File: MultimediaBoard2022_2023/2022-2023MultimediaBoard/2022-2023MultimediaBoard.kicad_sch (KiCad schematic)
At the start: 16 parts, among them J1 Conn_02x02_Counter_Clockwise_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, J2 RJ45_LED_Shielded_Ethernet, J3 Conn_02x03_Counter_Clockwise, U2 OKI, U3 Teensy4.1_DEV-16771

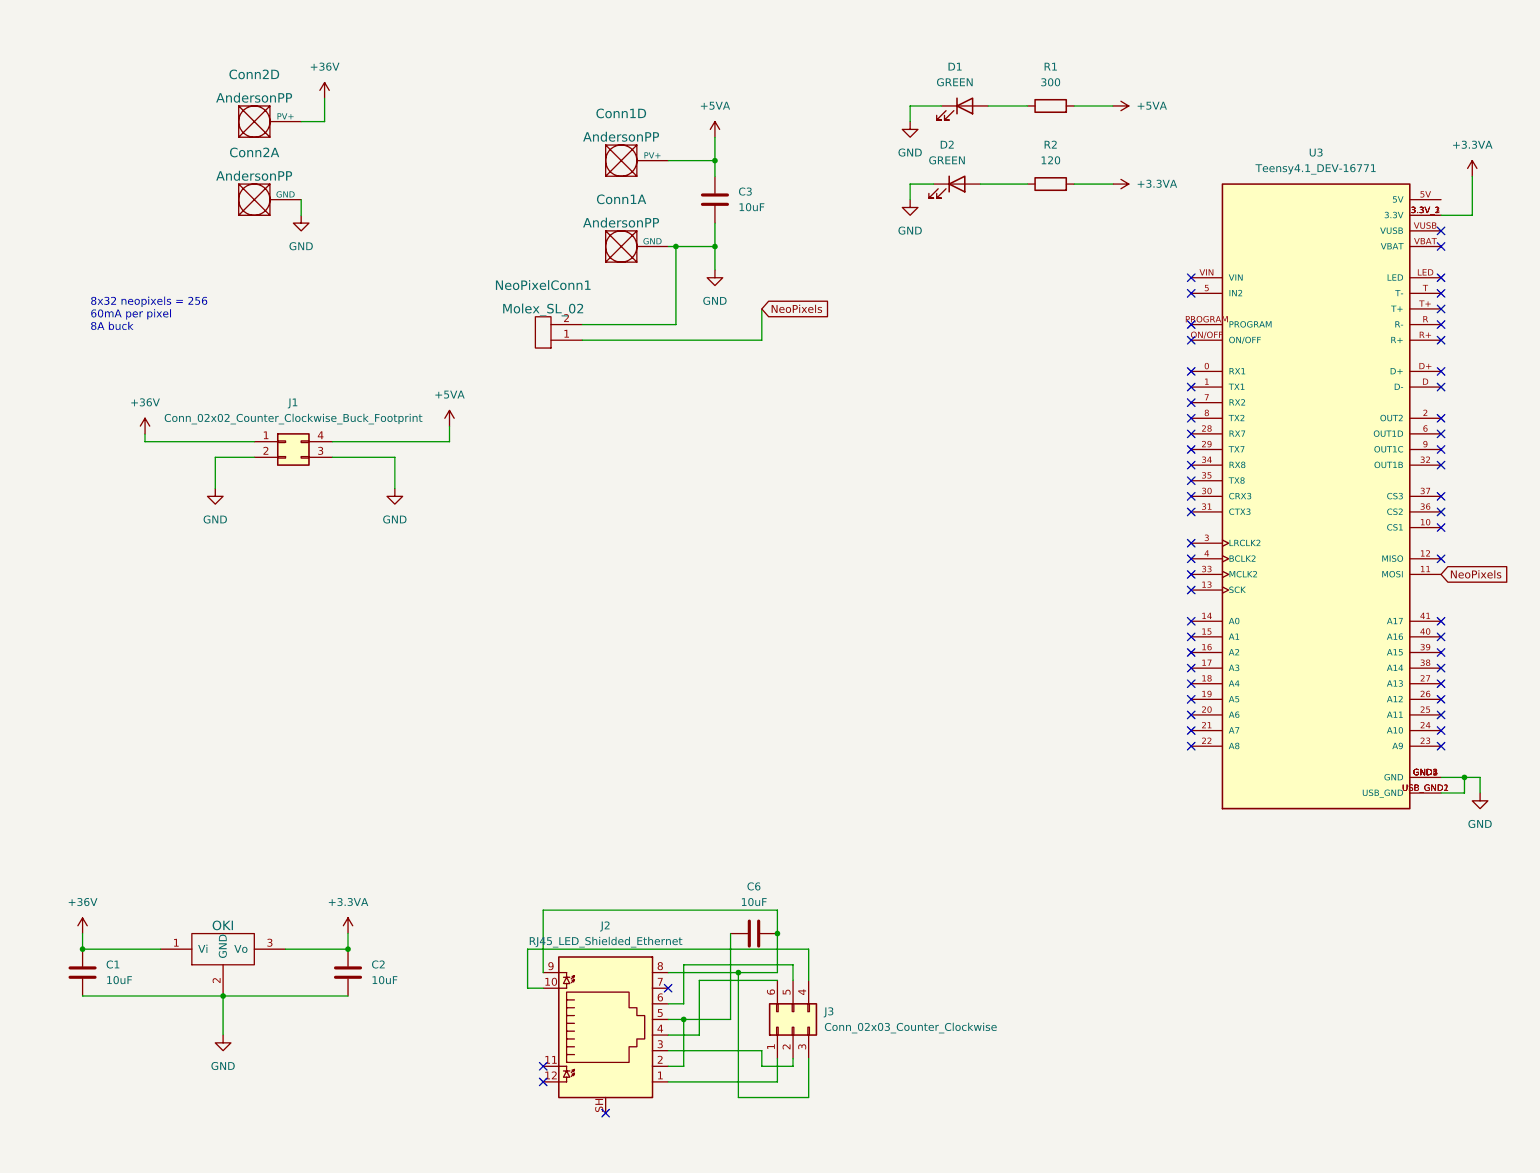
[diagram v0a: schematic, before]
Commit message: Sectioned parts of schematic, changed power sources, grounded LEDs
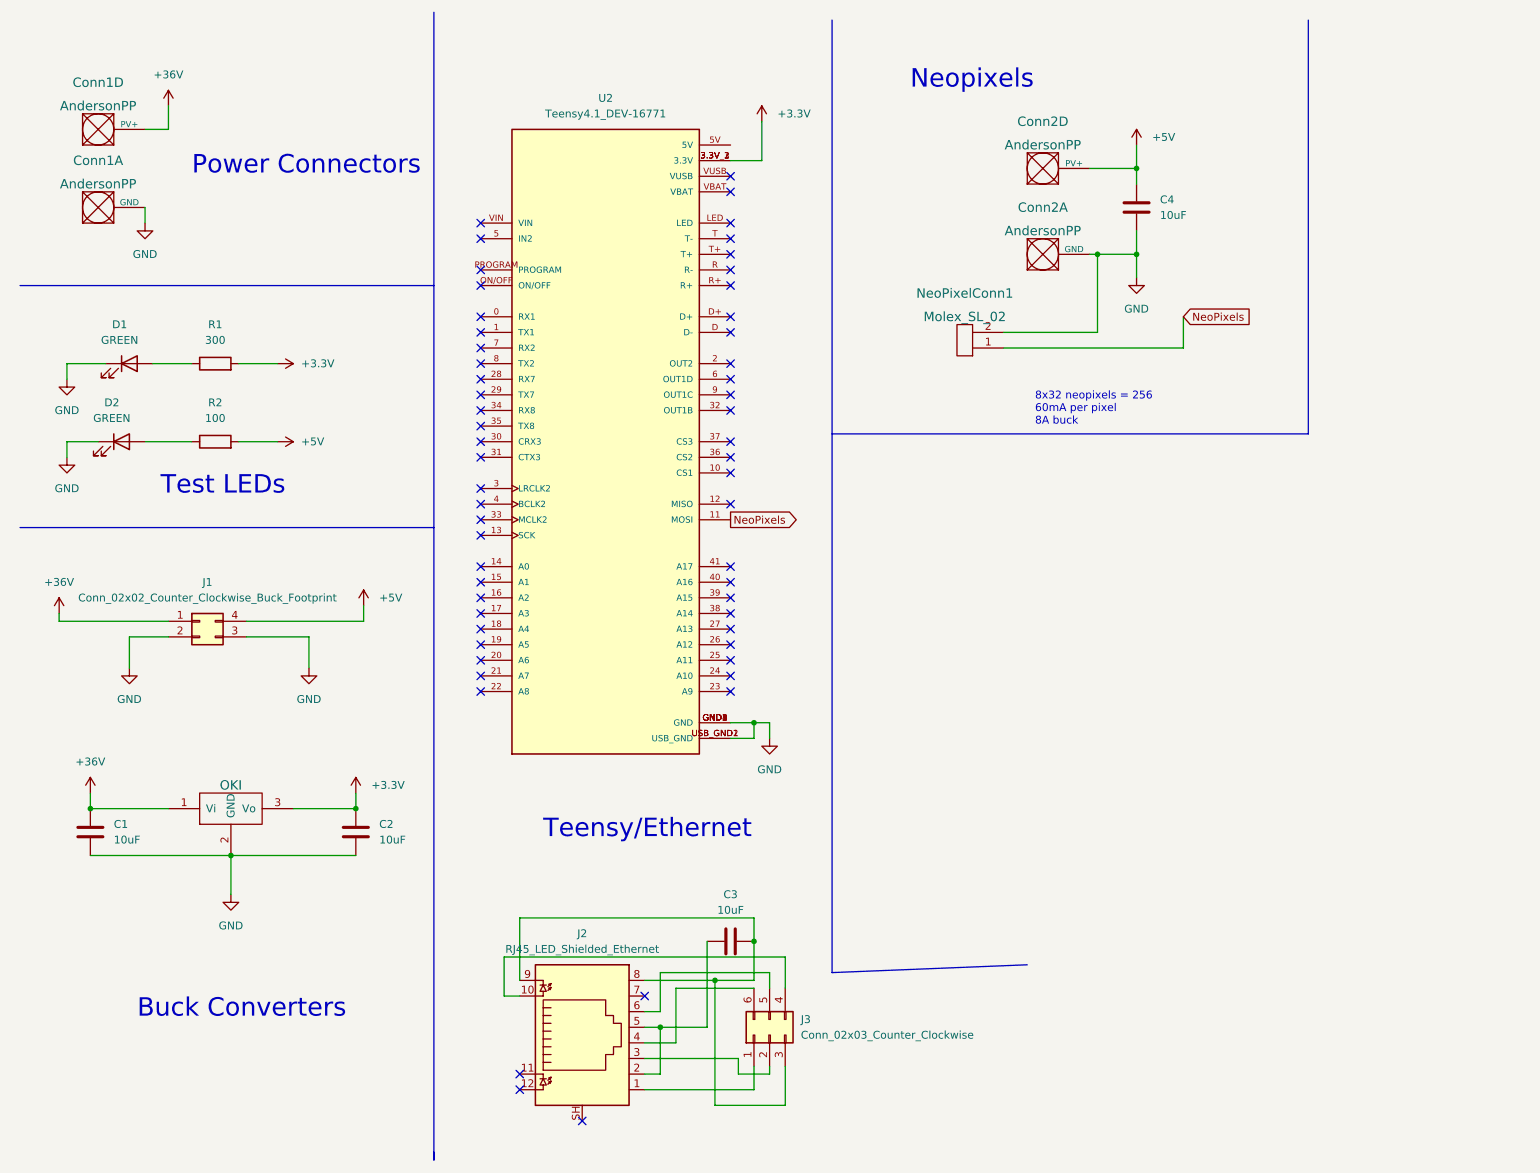
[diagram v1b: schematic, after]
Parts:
- removed C6: 10uF, Capacitor_SMD:C_0603_1608Metric_Pad1.08x0.95mm_HandSolder, symbol Device:C
- removed U2: OKI, MRDT_Devices:OKI_Horizontal, symbol MRDT_Devices:OKI
- removed U3: Teensy4.1_DEV-16771, MRDT_Shields:MODULE_DEV-16771, symbol MRDT_Shields:Teensy4.1_DEV-16771
- added C4: 10uF, symbol Device:C
- added U1: OKI, symbol MRDT_Devices:OKI
- added U2: Teensy4.1_DEV-16771, MODULE_DEV-16771, symbol MRDT_Shields:Teensy4.1_DEV-16771
- C1, C2, C3: footprint Capacitor_SMD:C_0603_1608Metric_Pad1.08x0.95mm_HandSolder -> (none)
- Conn1, Conn2: footprint MRDT_Connectors:Square_Anderson_2_H_Side_By_Side_PV -> (none)
- D1, D2: footprint LED_SMD:LED_0603_1608Metric_Pad1.05x0.95mm_HandSolder -> (none)
- J1: footprint Connector_PinHeader_2.00mm:PinHeader_2x02_P2.00mm_Vertical -> (none)
- J2: footprint MRDT_Connectors:RJ45_Teensy -> (none)
- J3: footprint Connector_PinHeader_2.00mm:PinHeader_2x03_P2.00mm_Vertical -> (none)
- NeoPixelConn1: footprint MRDT_Connectors:MOLEX_SL_02_Horizontal -> (none)
- R1: footprint Resistor_SMD:R_0201_0603Metric_Pad0.64x0.40mm_HandSolder -> (none)
- R2: value 120 -> 100; footprint Resistor_SMD:R_0201_0603Metric_Pad0.64x0.40mm_HandSolder -> (none)
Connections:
- net +36V: now also Conn1.4 (PV+), U1.1 (Vi); no longer Conn2.4 (PV+)
- net GND: now also C4.2, U1.2 (GND), U2.GND1 (GND), U2.GND2 (GND), U2.GND3 (GND), U2.GND4 (GND), U2.GND5 (GND), U2.USB_GND1 (USB_GND), U2.USB_GND2 (USB_GND); no longer C3.2
- net NeoPixels: now also U2.11 (MOSI)
- net at J2.8, J2.9, J3.3 (Pin_3): now also C3.1
- net at J2.2, J2.5: now also C3.2
- net +3.3VA renamed +3.3V
- net +3.3V: now also R1.2, U1.3 (Vo), U2.3.3V_1 (3.3V), U2.3.3V_2 (3.3V), U2.3.3V_3 (3.3V); no longer R2.2
- removed net +5VA: C3.1, Conn1.4 (PV+), J1.4 (Pin_4), R1.2
- new net +5V: C4.1, Conn2.4 (PV+), J1.4 (Pin_4), R2.2
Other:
- note added: "Buck Converters"
- note added: "Neopixels"
- note added: "Power Connectors"
- note added: "Teensy/Ethernet"
- note added: "Test LEDs"

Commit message: Renamed buck converter, minor touchups
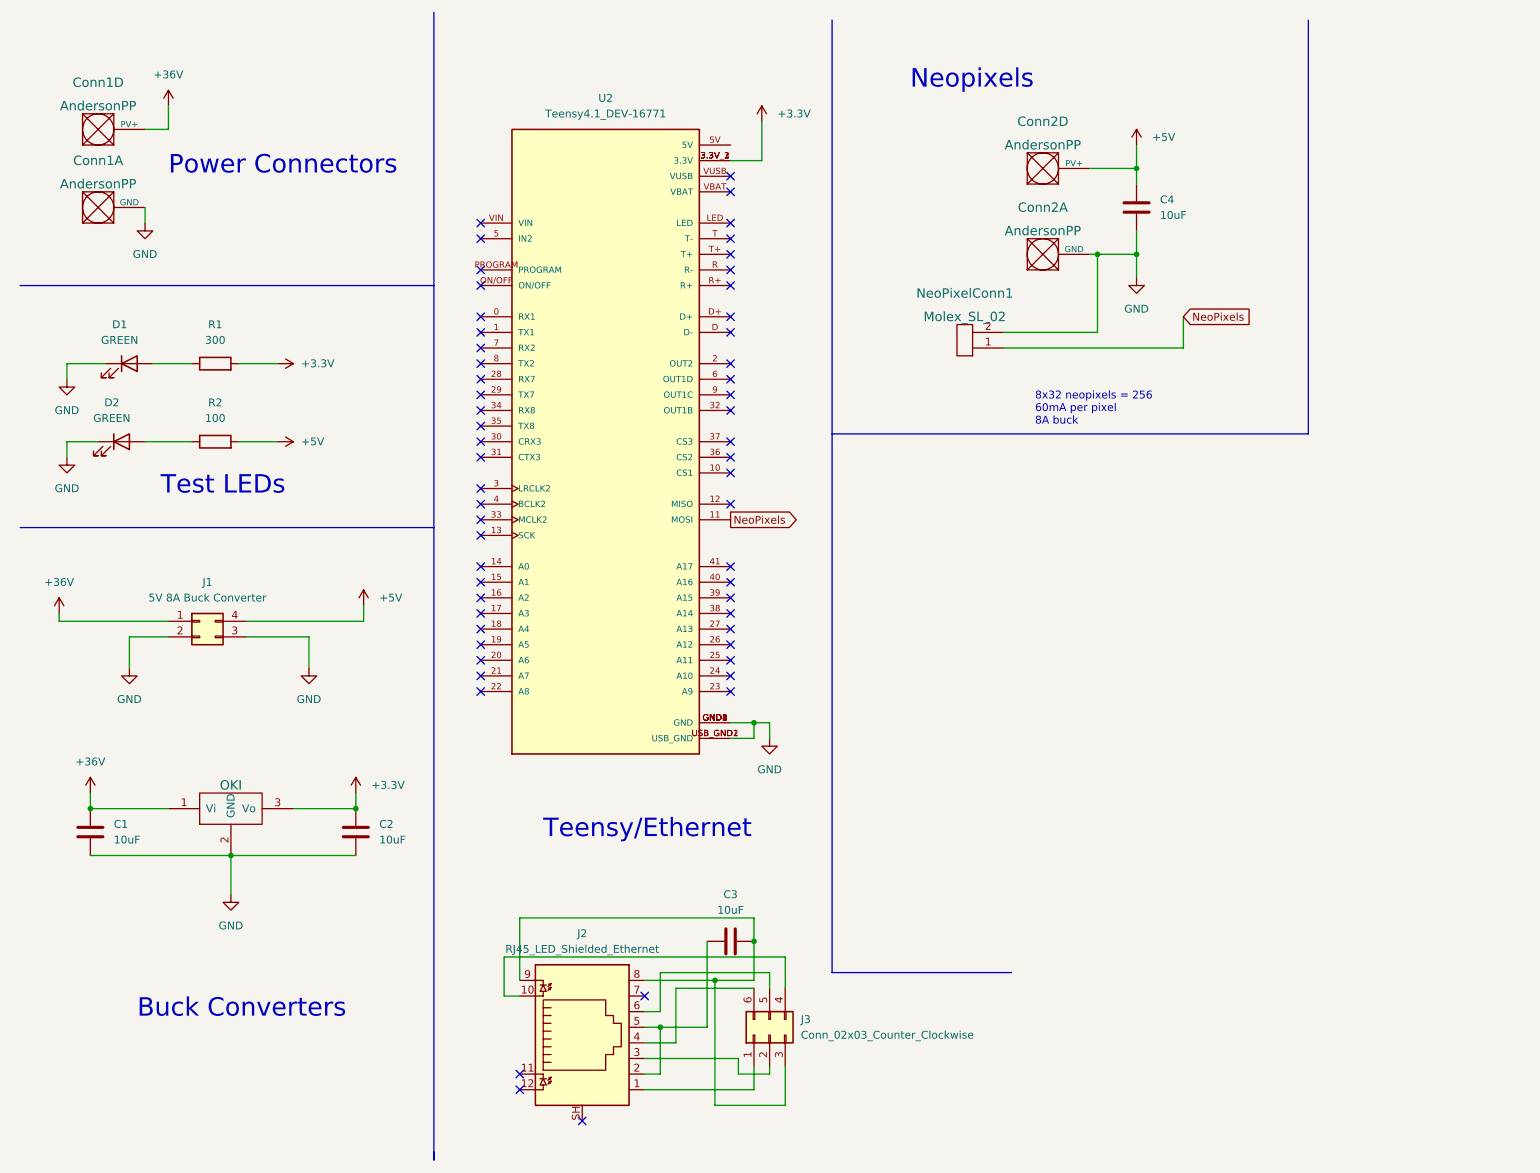
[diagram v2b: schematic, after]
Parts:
- J1: value Conn_02x02_Counter_Clockwise_Buck_Footprint -> 5V 8A Buck Converter
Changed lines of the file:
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@@
+    (stroke (width 0) (type default) (color 0 0 0 0))
+  )
+  (polyline (pts (xy 148.59 167.64) (xy 176.53 167.64))
     (stroke (width 0) (type default) (color 0 0 0 0))
   )
@@
     (stroke (width 0) (type default) (color 0 0 0 0))
   )
-  (polyline (pts (xy 147.32 167.64) (xy 179.07 166.37))
-    (stroke (width 0) (type default) (color 0 0 0 0))
-  )
   (wire (pts (xy 93.98 171.45) (xy 96.52 171.45))
     (stroke (width 0) (type default) (color 0 0 0 0))
@@
   )
   (wire (pts (xy 33.02 113.03) (xy 33.02 118.11))
+    (stroke (width 0) (type default) (color 0 0 0 0))
+  )
+  (polyline (pts (xy 147.32 167.64) (xy 148.59 167.64))
     (stroke (width 0) (type default) (color 0 0 0 0))
   )
@@
     (effects (font (size 3 3)) (justify left bottom))
   )
-  (text "Power Connectors" (at 43.18 38.1 0)
+  (text "Power Connectors" (at 39.37 38.1 0)
     (effects (font (size 3 3)) (justify left bottom))
   )
@@
     (in_bom yes) (on_board yes) (fields_autoplaced)
     (property "Reference" "J1" (id 0) (at 45.72 104.14 0))
-    (property "Value" "Conn_02x02_Counter_Clockwise_Buck_Footprint" (id 1) (at 45.72 106.68 0))
+    (property "Value" "5V 8A Buck Converter" (id 1) (at 45.72 106.68 0))
     (property "Footprint" "" (id 2) (at 44.45 110.49 0)
       (effects (font (size 1.27 1.27)) hide)
@@
     )
     (path "/9e2b21a3-05cc-4e86-bc90-cb131a45fd36"
-      (reference "J1") (unit 1) (value "Conn_02x02_Counter_Clockwise_Buck_Footprint") (footprint "")
+      (reference "J1") (unit 1) (value "5V 8A Buck Converter") (footprint "")
     )
     (path "/01d7ed54-9442-442b-bc84-39ad0e7c7375"

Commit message: Quick fixes, new BOM
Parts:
- C1: renamed from C4; footprint (none) -> Capacitor_SMD:C_0603_1608Metric_Pad1.08x0.95mm_HandSolder
- C2: renamed from C1; footprint (none) -> Capacitor_SMD:C_0603_1608Metric_Pad1.08x0.95mm_HandSolder
- C3: renamed from C2; footprint (none) -> Capacitor_SMD:C_0603_1608Metric_Pad1.08x0.95mm_HandSolder
- C4: renamed from C3; footprint (none) -> Capacitor_SMD:C_0603_1608Metric_Pad1.08x0.95mm_HandSolder
- Conn1, Conn2: footprint (none) -> MRDT_Connectors:Square_Anderson_2_H_Side_By_Side_PV
- D1, D2: footprint (none) -> LED_SMD:LED_0603_1608Metric_Pad1.05x0.95mm_HandSolder
- J1: footprint (none) -> Connector_PinHeader_2.00mm:PinHeader_2x02_P2.00mm_Vertical
- J2: renamed from J3; footprint (none) -> Connector_PinHeader_2.00mm:PinHeader_2x03_P2.00mm_Vertical
- J3: renamed from J2; footprint (none) -> MRDT_Connectors:RJ45_Teensy
- NeoPixelConn1: footprint (none) -> MRDT_Connectors:MOLEX_SL_02_Horizontal
- R1, R2: footprint (none) -> Resistor_SMD:R_0201_0603Metric_Pad0.64x0.40mm_HandSolder
- U1: renamed from U2; footprint MODULE_DEV-16771 -> MRDT_Shields:Teensy_4_1_Vertical
- U2: renamed from U1; footprint (none) -> MRDT_Devices:OKI_Horizontal
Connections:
- net Tx+: now reaches J2.1 (Pin_1), J3.1
- net Tx-: now reaches J2.2 (Pin_2), J3.3
- net Rx+: now reaches J2.6 (Pin_6), J3.4
- net Rx-: now reaches J2.5 (Pin_5), J3.6
- no-connect marks 57 -> 58
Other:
- moved on the sheet: Conn1D, U1

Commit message: PCB edits and footprint assignment
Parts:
- J1: footprint Connector_PinHeader_2.00mm:PinHeader_2x02_P2.00mm_Vertical -> MultimediaBoard2023:5V 8A Buck Converter
- R1, R2: footprint Resistor_SMD:R_0201_0603Metric_Pad0.64x0.40mm_HandSolder -> Resistor_SMD:R_0603_1608Metric_Pad0.98x0.95mm_HandSolder
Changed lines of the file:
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@@
     (property "Reference" "R2" (id 0) (at 46.99 74.93 90))
     (property "Value" "100" (id 1) (at 46.99 77.47 90))
-    (property "Footprint" "Resistor_SMD:R_0201_0603Metric_Pad0.64x0.40mm_HandSolder" (id 2) (at 46.99 83.058 90)
+    (property "Footprint" "Resistor_SMD:R_0603_1608Metric_Pad0.98x0.95mm_HandSolder" (id 2) (at 46.99 83.058 90)
       (effects (font (size 1.27 1.27)) hide)
     )
@@
     (property "Reference" "R1" (id 0) (at 46.99 62.23 90))
     (property "Value" "300" (id 1) (at 46.99 64.77 90))
-    (property "Footprint" "Resistor_SMD:R_0201_0603Metric_Pad0.64x0.40mm_HandSolder" (id 2) (at 46.99 70.358 90)
+    (property "Footprint" "Resistor_SMD:R_0603_1608Metric_Pad0.98x0.95mm_HandSolder" (id 2) (at 46.99 70.358 90)
       (effects (font (size 1.27 1.27)) hide)
     )
@@
     (property "Reference" "J1" (id 0) (at 45.72 104.14 0))
     (property "Value" "5V 8A Buck Converter" (id 1) (at 45.72 106.68 0))
-    (property "Footprint" "Connector_PinHeader_2.00mm:PinHeader_2x02_P2.00mm_Vertical" (id 2) (at 44.45 110.49 0)
+    (property "Footprint" "MultimediaBoard2023:5V 8A Buck Converter" (id 2) (at 44.45 110.49 0)
       (effects (font (size 1.27 1.27)) hide)
     )
@@
     )
     (path "/9e2b21a3-05cc-4e86-bc90-cb131a45fd36"
-      (reference "J1") (unit 1) (value "5V 8A Buck Converter") (footprint "Connector_PinHeader_2.00mm:PinHeader_2x02_P2.00mm_Vertical")
+      (reference "J1") (unit 1) (value "5V 8A Buck Converter") (footprint "MultimediaBoard2023:5V 8A Buck Converter")
     )
     (path "/62d412ba-15cd-4cce-99c3-088b9b33c569"
@@
     )
     (path "/8cbe023b-f19d-4143-aabf-b101849d944d"
-      (reference "R1") (unit 1) (value "300") (footprint "Resistor_SMD:R_0201_0603Metric_Pad0.64x0.40mm_HandSolder")
+      (reference "R1") (unit 1) (value "300") (footprint "Resistor_SMD:R_0603_1608Metric_Pad0.98x0.95mm_HandSolder")
     )
     (path "/233062e8-6ddf-4b91-b479-049ab48c6ebe"
-      (reference "R2") (unit 1) (value "100") (footprint "Resistor_SMD:R_0201_0603Metric_Pad0.64x0.40mm_HandSolder")
+      (reference "R2") (unit 1) (value "100") (footprint "Resistor_SMD:R_0603_1608Metric_Pad0.98x0.95mm_HandSolder")
     )
     (path "/12705423-3c75-43d4-8693-5750f511a878"

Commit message: Layout updates
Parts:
- removed C2, C3: 10uF, Capacitor_SMD:C_0603_1608Metric_Pad1.08x0.95mm_HandSolder, symbol Device:C
- removed D1: GREEN, LED_SMD:LED_0603_1608Metric_Pad1.05x0.95mm_HandSolder, symbol Device:LED
- removed R1: 300, Resistor_SMD:R_0603_1608Metric_Pad0.98x0.95mm_HandSolder, symbol Device:R
- removed U2: OKI, MRDT_Devices:OKI_Horizontal, symbol MRDT_Devices:OKI
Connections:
- net +5V: now also U1.VIN
- net GND: now also J3.SH
- net +3.3V: no longer names the net of U1.3.3V_1 (3.3V), U1.3.3V_2 (3.3V), U1.3.3V_3 (3.3V)
- no-connect marks 58 -> 57
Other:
- moved on the sheet: C1, Conn2A, Conn2D, NeoPixelConn1
